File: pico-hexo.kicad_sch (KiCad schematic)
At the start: 18 parts, among them J1 USB_A, U1 RP2040, Y1 24MHz

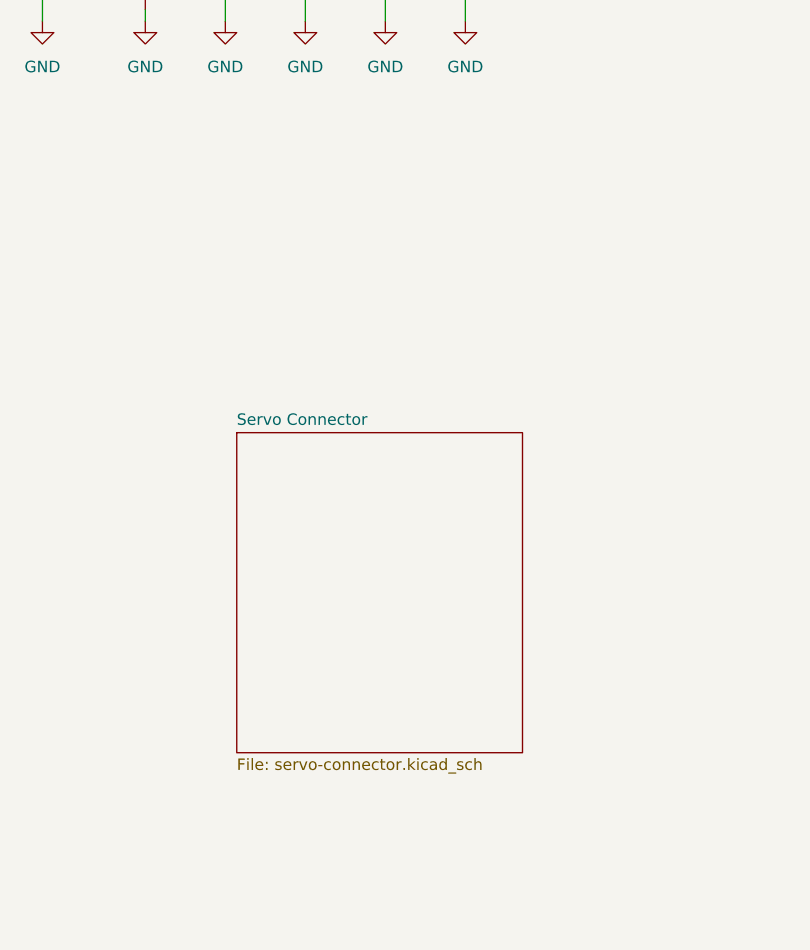
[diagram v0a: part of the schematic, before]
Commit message: Added servo-connector, BNO055, power (not finished)
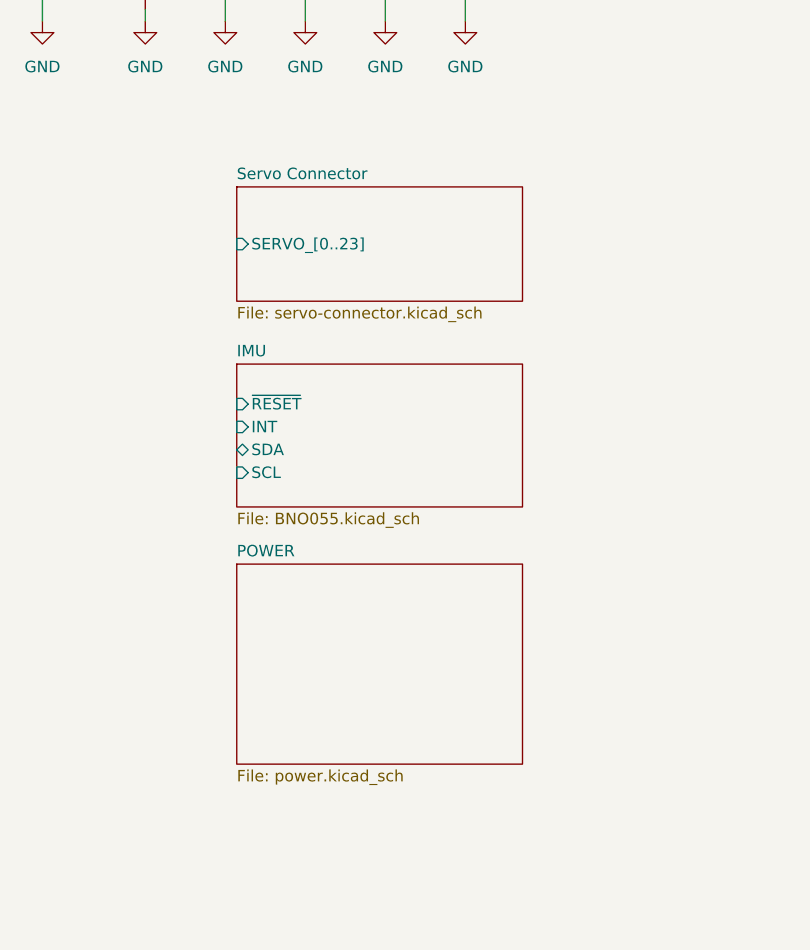
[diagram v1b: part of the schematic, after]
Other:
- added sheet IMU (BNO055.kicad_sch)
- added sheet POWER (power.kicad_sch)
- sheet Servo Connector ports: added SERVO_[0..23]; removed none
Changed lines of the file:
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@@
 	(label "GPIO13"
 		(at 152.4 102.87 180)
+		(fields_autoplaced yes)
 		(effects
 			(font
@@
 	(label "GPIO16"
 		(at 152.4 110.49 180)
+		(fields_autoplaced yes)
 		(effects
 			(font
@@
 	(label "GPIO18"
 		(at 152.4 115.57 180)
+		(fields_autoplaced yes)
 		(effects
 			(font
@@
 	(label "GPIO2"
 		(at 152.4 74.93 180)
+		(fields_autoplaced yes)
 		(effects
 			(font
@@
 	(label "GPIO11"
 		(at 152.4 97.79 180)
+		(fields_autoplaced yes)
 		(effects
 			(font
@@
 	(label "GPIO0"
 		(at 152.4 69.85 180)
+		(fields_autoplaced yes)
 		(effects
 			(font
@@
 	(label "USB_DP"
 		(at 81.28 77.47 0)
+		(fields_autoplaced yes)
 		(effects
 			(font
@@
 	(label "GPIO25"
 		(at 152.4 133.35 180)
+		(fields_autoplaced yes)
 		(effects
 			(font
@@
 	(label "SWD"
 		(at 82.55 138.43 0)
+		(fields_autoplaced yes)
 		(effects
 			(font
@@
 	(label "SWCLK"
 		(at 82.55 135.89 0)
+		(fields_autoplaced yes)
 		(effects
 			(font
@@
 	(label "USB_DN"
 		(at 81.28 80.01 0)
+		(fields_autoplaced yes)
 		(effects
 			(font
@@
 	(label "GPIO21"
 		(at 152.4 123.19 180)
+		(fields_autoplaced yes)
 		(effects
 			(font
@@
 	(label "GPIO28_ADC2"
 		(at 152.4 143.51 180)
+		(fields_autoplaced yes)
 		(effects
 			(font
@@
 	(label "GPIO4"
 		(at 152.4 80.01 180)
+		(fields_autoplaced yes)
 		(effects
 			(font
@@
 	(label "QSPI_SS"
 		(at 78.74 87.63 0)
+		(fields_autoplaced yes)
 		(effects
 			(font
@@
 	(label "QSPI_SD0"
 		(at 78.74 92.71 0)
+		(fields_autoplaced yes)
 		(effects
 			(font
@@
 	(label "GPIO3"
 		(at 152.4 77.47 180)
+		(fields_autoplaced yes)
 		(effects
 			(font
@@
 	(label "GPIO26_ADC0"
 		(at 152.4 138.43 180)
+		(fields_autoplaced yes)
 		(effects
 			(font
@@
 	(label "GPIO8"
 		(at 152.4 90.17 180)
+		(fields_autoplaced yes)
 		(effects
 			(font
@@
 	(label "GPIO10"
 		(at 152.4 95.25 180)
+		(fields_autoplaced yes)
 		(effects
 			(font
@@
 	(label "GPIO24"
 		(at 152.4 130.81 180)
+		(fields_autoplaced yes)
 		(effects
 			(font
@@
 	(label "GPIO20"
 		(at 152.4 120.65 180)
+		(fields_autoplaced yes)
 		(effects
 			(font
@@
 	(label "GPIO1"
 		(at 152.4 72.39 180)
+		(fields_autoplaced yes)
 		(effects
 			(font
@@
 	(label "QSPI_SCLK"
 		(at 78.74 102.87 0)
+		(fields_autoplaced yes)
 		(effects
 			(font
@@
 	(label "GPIO5"
 		(at 152.4 82.55 180)
+		(fields_autoplaced yes)
 		(effects
 			(font
@@
 	(label "GPIO22"
 		(at 152.4 125.73 180)
+		(fields_autoplaced yes)
 		(effects
 			(font
@@
 	(label "GPIO23"
 		(at 152.4 128.27 180)
+		(fields_autoplaced yes)
 		(effects
 			(font
@@
 	(label "GPIO15"
 		(at 152.4 107.95 180)
+		(fields_autoplaced yes)
 		(effects
 			(font
@@
 	(label "RUN"
 		(at 83.82 69.85 0)
+		(fields_autoplaced yes)
 		(effects
 			(font
@@
 	(label "QSPI_SD3"
 		(at 78.74 100.33 0)
+		(fields_autoplaced yes)
 		(effects
 			(font
@@
 	(label "GPIO12"
 		(at 152.4 100.33 180)
+		(fields_autoplaced yes)
 		(effects
 			(font
@@
 	(label "GPIO27_ADC1"
 		(at 152.4 140.97 180)
+		(fields_autoplaced yes)
 		(effects
 			(font
@@
 	(label "GPIO7"
 		(at 152.4 87.63 180)
+		(fields_autoplaced yes)
 		(effects
 			(font
@@
 	(label "GPIO19"
 		(at 152.4 118.11 180)
+		(fields_autoplaced yes)
 		(effects
 			(font
@@
 	(label "GPIO9"
 		(at 152.4 92.71 180)
+		(fields_autoplaced yes)
 		(effects
 			(font
@@
 	(label "GPIO29_ADC3"
 		(at 152.4 146.05 180)
+		(fields_autoplaced yes)
 		(effects
 			(font
@@
 	(label "GPIO6"
 		(at 152.4 85.09 180)
+		(fields_autoplaced yes)
 		(effects
 			(font
@@
 	(label "QSPI_SD2"
 		(at 78.74 97.79 0)
+		(fields_autoplaced yes)
 		(effects
 			(font
@@
 	(label "QSPI_SD1"
 		(at 78.74 95.25 0)
+		(fields_autoplaced yes)
 		(effects
 			(font
@@
 	(label "GPIO14"
 		(at 152.4 105.41 180)
+		(fields_autoplaced yes)
 		(effects
 			(font
@@
 	(label "GPIO17"
 		(at 152.4 113.03 180)
+		(fields_autoplaced yes)
 		(effects
 			(font
@@
 	)
 	(sheet
-		(at 185.42 93.98)
-		(size 31.75 35.56)
+		(at 185.42 66.675)
+		(size 31.75 12.7)
 		(fields_autoplaced yes)
 		(stroke
@@
 		)
 		(property "Sheetname" "Servo Connector"
-			(at 185.42 93.2684 0)
+			(at 185.42 65.9634 0)
 			(effects
 				(font
@@
 		)
 		(property "Sheetfile" "servo-connector.kicad_sch"
-			(at 185.42 130.1246 0)
+			(at 185.42 79.9596 0)
 			(effects
 				(font
@@
 			)
 		)
+		(pin "SERVO_[0..23]" input
+			(at 185.42 73.025 180)
+			(effects
+				(font
+					(size 1.27 1.27)
+				)
+				(justify left)
+			)
+		)
 		(instances
 			(project "pico-hexo"
@@
 				)
 			)
+		)
+	)
+	(sheet
+		(at 185.42 108.585)
+		(size 31.75 22.225)
+		(fields_autoplaced yes)
+		(stroke
+			(width 0.1524)
+			(type solid)
+		)
+		(fill
+			(color 0 0 0 0.0000)
+		)
+		(property "Sheetname" "POWER"
+			(at 185.42 107.8734 0)
+			(effects
+				(font
+					(size 1.27 1.27)
+				)
+				(justify left bottom)
+			)
+		)
+		(property "Sheetfile" "power.kicad_sch"
+			(at 185.42 131.3946 0)
+			(effects
+				(font
+					(size 1.27 1.27)
+				)
+				(justify left top)
+			)
+		)
+		(instances
+			(project "pico-hexo"
+				(path "/249a9a7e-a950-4b1e-ad7d-a9cd3a27279c"
+					(page "4")
+				)
+			)
+		)
+	)
+	(sheet
+		(at 185.42 86.36)
+		(size 31.75 15.875)
+		(fields_autoplaced yes)
+		(stroke
+			(width 0.1524)
+			(type solid)
+		)
+		(fill
+			(color 0 0 0 0.0000)
+		)
+		(property "Sheetname" "IMU"
+			(at 185.42 85.6484 0)
+			(effects
+				(font
+					(size 1.27 1.27)
+				)
+				(justify left bottom)
+			)
+		)
+		(property "Sheetfile" "BNO055.kicad_sch"
+			(at 185.42 102.8196 0)
+			(effects
+				(font
+					(size 1.27 1.27)
+				)
+				(justify left top)
+			)
+		)
+		(pin "INT" input
+			(at 185.42 93.345 180)
+			(effects
+				(font
+					(size 1.27 1.27)
+				)
+				(justify left)
+			)
+		)
+		(pin "SDA" bidirectional
+			(at 185.42 95.885 180)
+			(effects
+				(font
+					(size 1.27 1.27)
+				)
+				(justify left)
+			)
+		)
+		(pin "~{RESET}" input
+			(at 185.42 90.805 180)
+			(effects
+				(font
+					(size 1.27 1.27)
+				)
+				(justify left)
+			)
+		)
+		(pin "SCL" input
+			(at 185.42 98.425 180)
+			(effects
+				(font
+					(size 1.27 1.27)
+				)
+				(justify left)
+			)
+		)
+		(instances
+			(project "pico-hexo"
+				(path "/249a9a7e-a950-4b1e-ad7d-a9cd3a27279c"
+					(page "3")
+				)
+			)

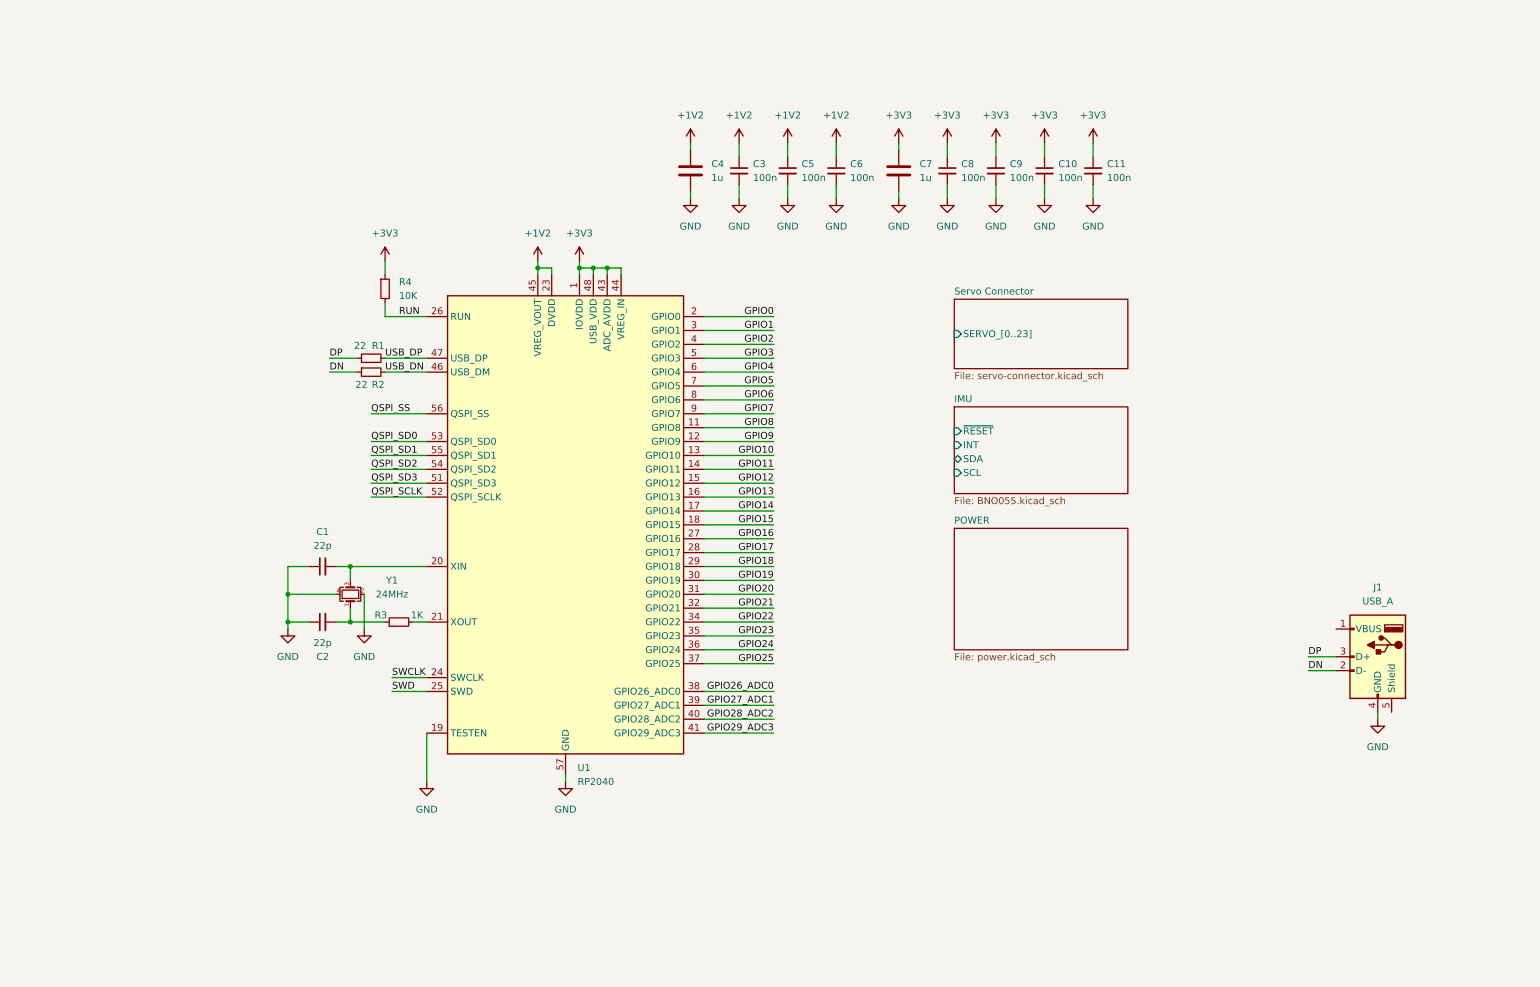
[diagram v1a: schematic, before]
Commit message: Add zener to each servo pin, add I2C and UART connector
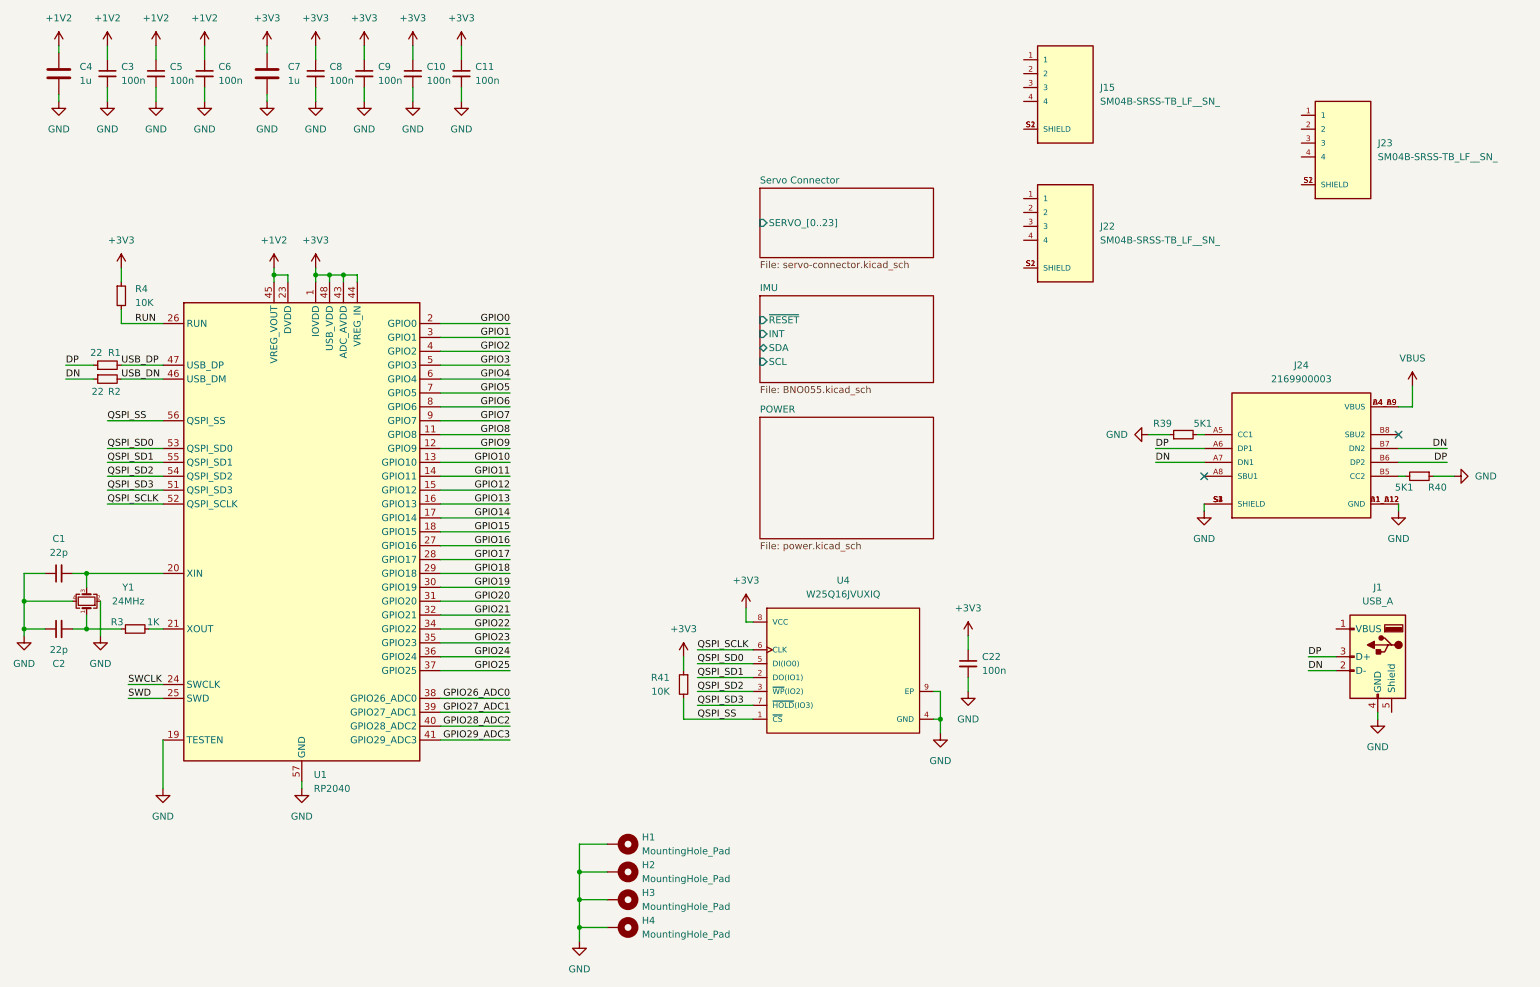
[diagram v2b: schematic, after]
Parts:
- added C22: 100n, Capacitor_SMD:C_0402_1005Metric, symbol Device:C_Small
- added H1, H2, H3, H4: MountingHole_Pad, MountingHole:MountingHole_3.2mm_M3_Pad_Via, symbol Mechanical:MountingHole_Pad
- added J15, J22, J23: SM04B-SRSS-TB_LF__SN_, SM04B-SRSS-TB_LF__SN_:JST_SM04B-SRSS-TB_LF__SN_, symbol SM04B-SRSS-TB_LF__SN_:SM04B-SRSS-TB_LF__SN_
- added J24: 2169900003, Molex-USB-mid-mount-2169900003:MOLEX_2169900003, symbol 2169900003:2169900003
- added R39, R40: 5K1, Resistor_SMD:R_0402_1005Metric, symbol Device:R_Small
- added R41: 10K, Resistor_SMD:R_0402_1005Metric, symbol Device:R_Small
- added U4: W25Q16JVUXIQ, W25Q16JVUXIQ:Winbond-UX-0-0-IPC_B, symbol W25Q16JVUXIQ:W25Q16JVUXIQ
- C1, C10, C11, C2, C3, C5, C6, C8, C9: footprint (none) -> Capacitor_SMD:C_0402_1005Metric
- C4, C7: footprint (none) -> Capacitor_SMD:C_0603_1608Metric
- J1: footprint (none) -> Connector_USB:USB_A_Molex_67643_Horizontal
- R1, R2, R3, R4: footprint (none) -> Resistor_SMD:R_0402_1005Metric
- Y1: footprint (none) -> Crystal:Crystal_SMD_3225-4Pin_3.2x2.5mm
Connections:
- net +3V3: now also C22.1, R41.1, U4.8 (VCC)
- net DN: now also J24.A7 (DN1), J24.B7 (DN2)
- net DP: now also J24.A6 (DP1), J24.B6 (DP2)
- net GND: now also C22.2, H1.1, H2.1, H3.1, H4.1, J24.A1_B12 (GND), J24.B1_A12 (GND), J24.S1 (SHIELD), J24.S2 (SHIELD), J24.S3 (SHIELD), J24.S4 (SHIELD), R39.1, R40.1, U4.4 (GND), U4.9 (EP)
- net QSPI_SCLK: now also U4.6 (CLK)
- net QSPI_SD0: now also U4.5 (DI(IO0))
- net QSPI_SD1: now also U4.2 (DO(IO1))
- net QSPI_SD2: now also U4.3 (~{WP}(IO2))
- net QSPI_SD3: now also U4.7 (~{HOLD}(IO3))
- net QSPI_SS: now also R41.2, U4.1 (~{CS})
- new net: J22.S1 (SHIELD), J22.S2 (SHIELD)
- new net: J15.S1 (SHIELD), J15.S2 (SHIELD)
- new net: J24.A5 (CC1), R39.2
- new net: J24.B5 (CC2), R40.2
- new net: J23.S1 (SHIELD), J23.S2 (SHIELD)
- new net VBUS: J24.A4_B9 (VBUS), J24.B4_A9 (VBUS)
- no-connect marks 0 -> 2
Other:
- moved on the sheet: C1, C10, C11, C2, C3, C4, C5, C6, C7, C8, C9, R1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
